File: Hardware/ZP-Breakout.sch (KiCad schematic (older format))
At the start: 5 parts

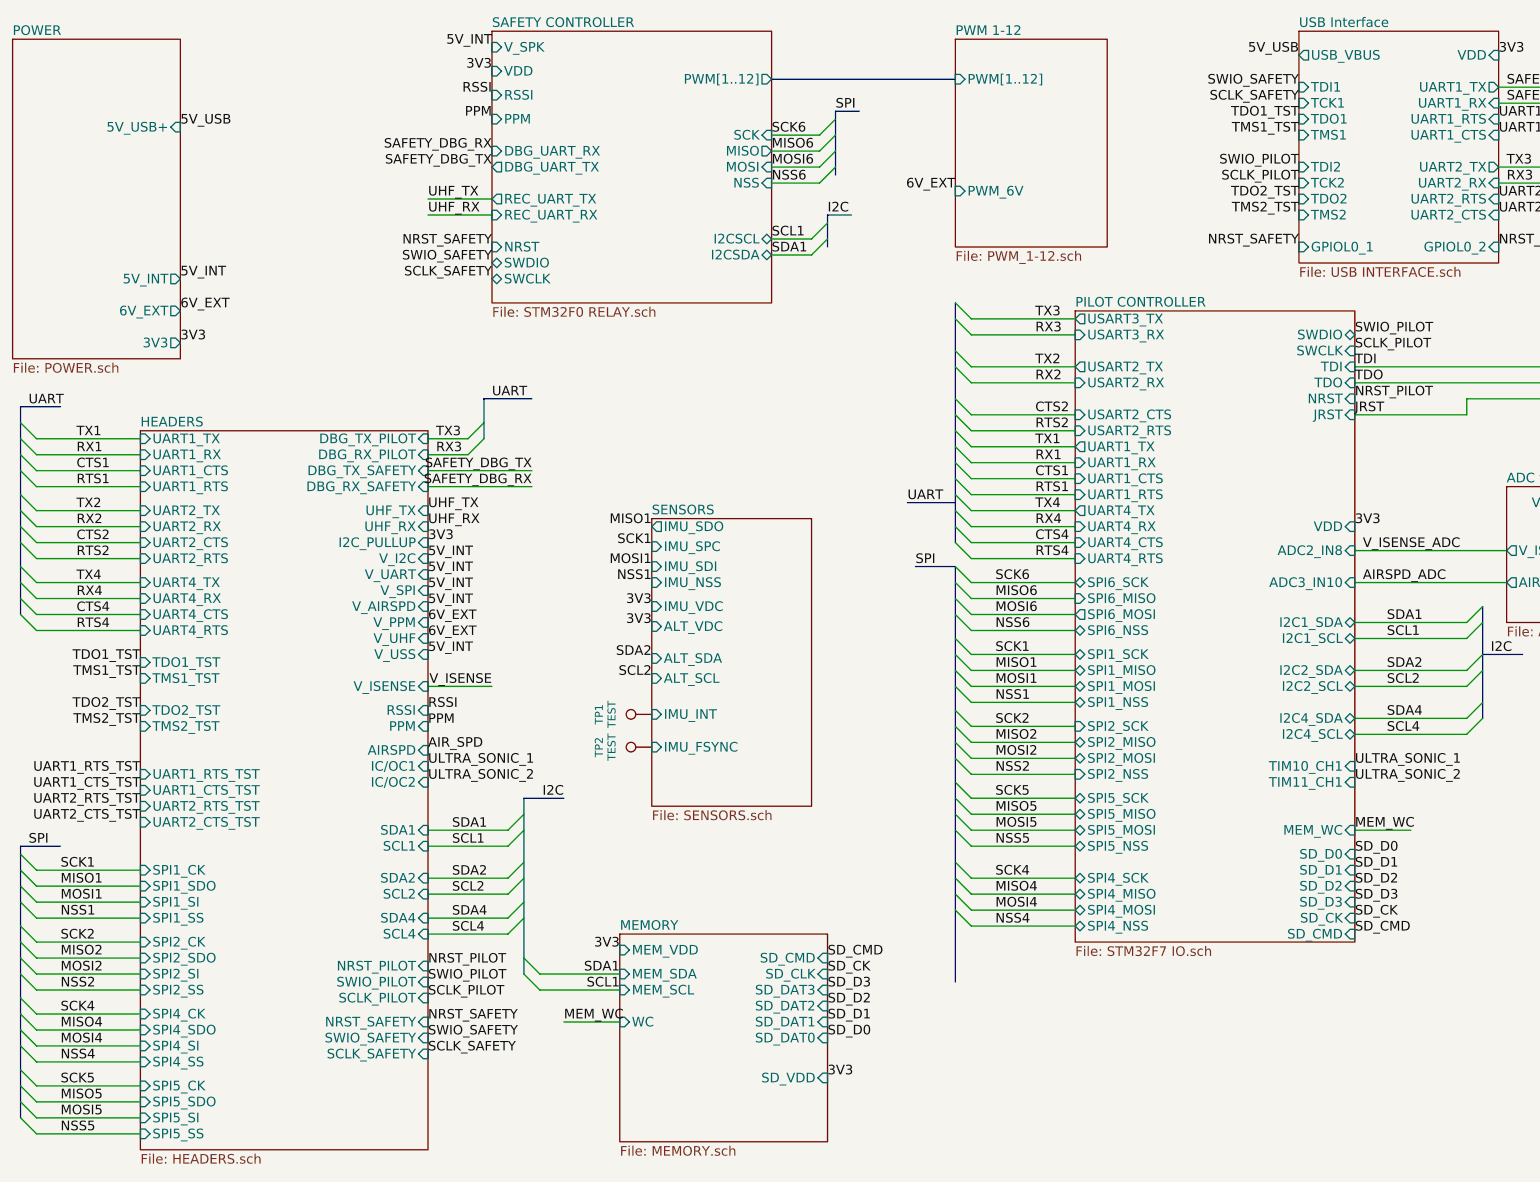
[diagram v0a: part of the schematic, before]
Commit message: Added additional headers to some interfaces, GPIOs, and FTDI pins. Added silks
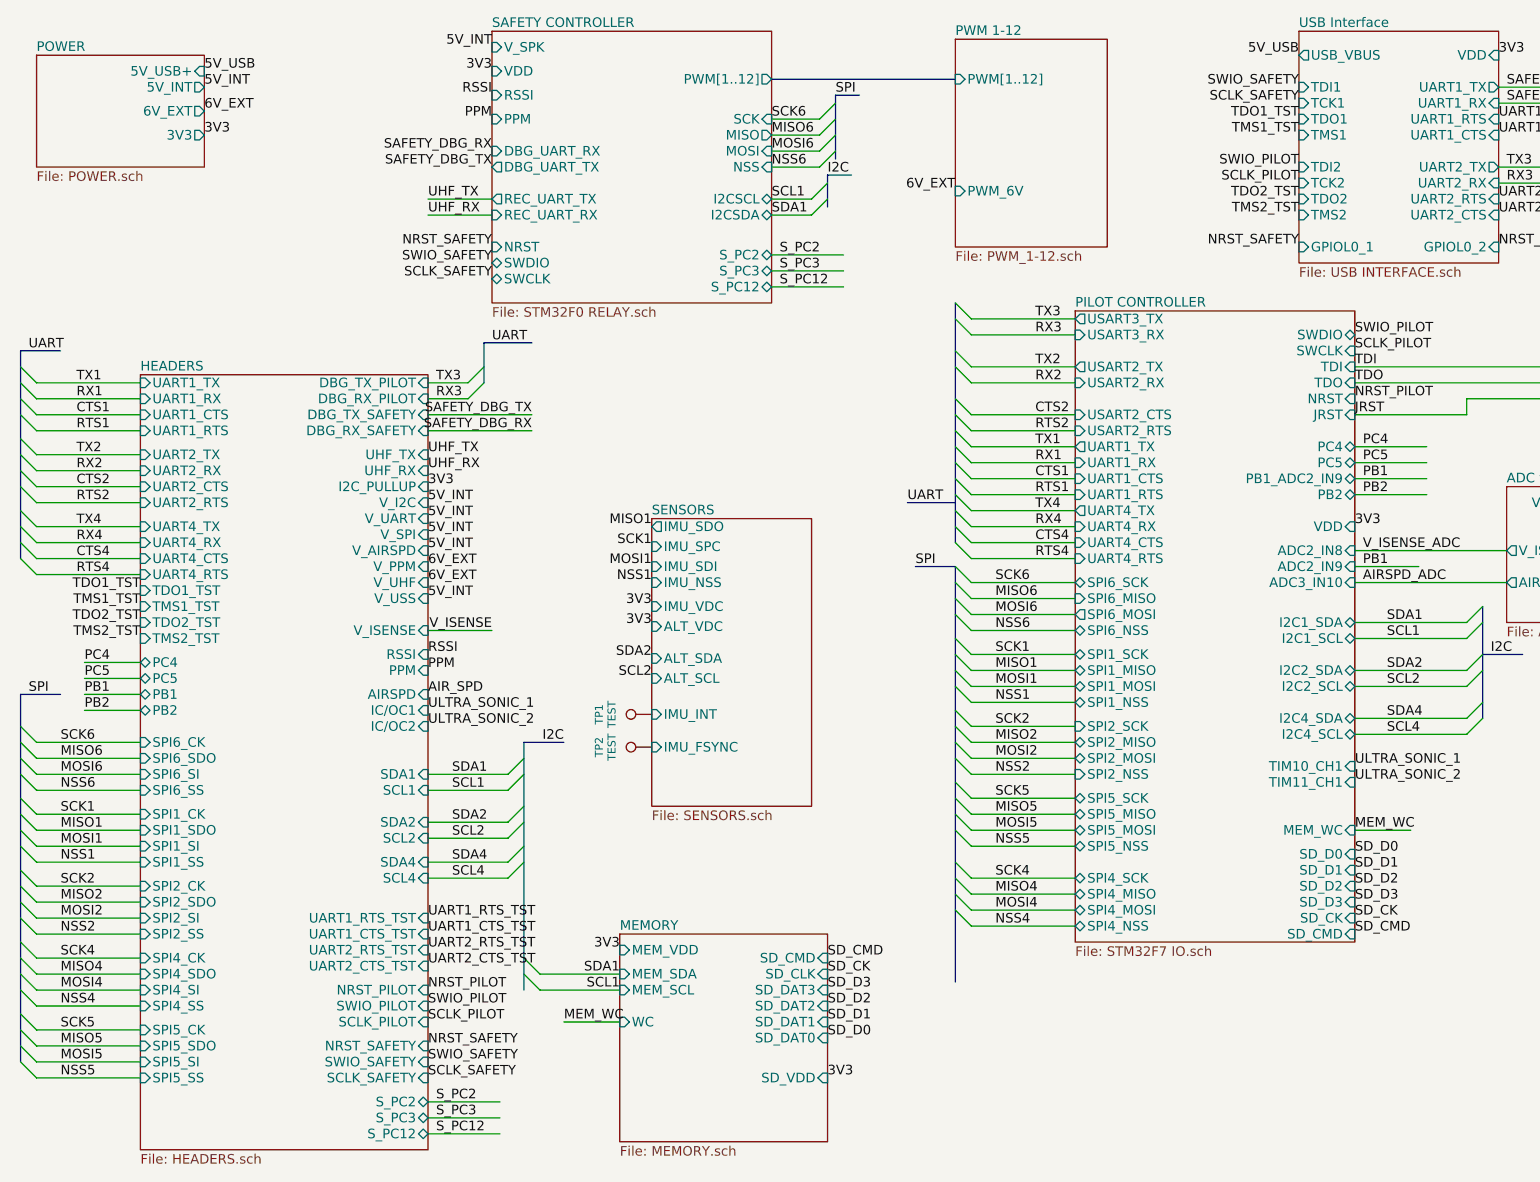
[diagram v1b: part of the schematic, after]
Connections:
- net labels added: PB1, PB2, PC4, PC5, S_PC12, S_PC2, S_PC3
- wire segments 102 -> 121
